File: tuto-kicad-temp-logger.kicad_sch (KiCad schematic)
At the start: 0 parts

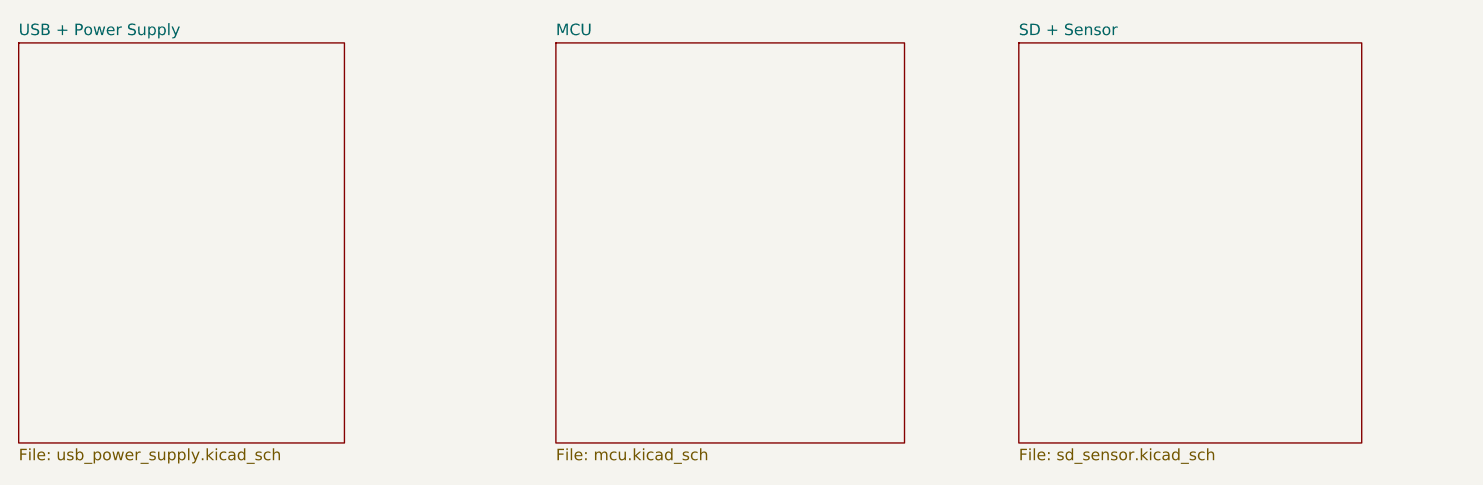
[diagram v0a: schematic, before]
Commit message: Connexion des pages du schéma
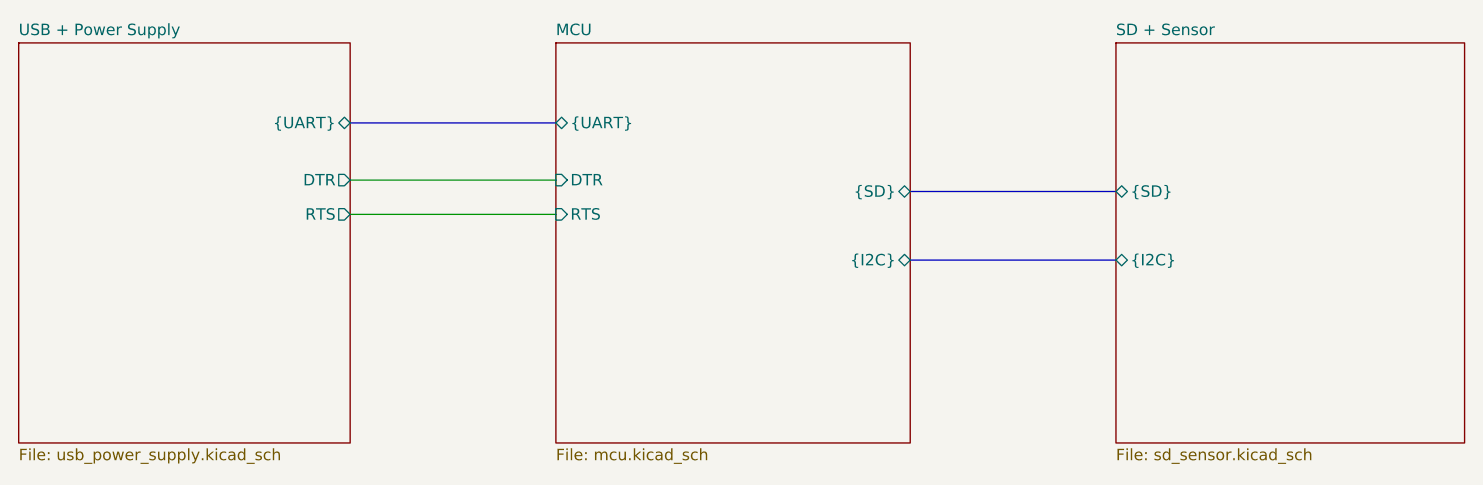
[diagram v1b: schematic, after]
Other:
- sheet MCU ports: added DTR, RTS, {I2C}, {SD}, {UART}; removed none
- sheet SD + Sensor ports: added {I2C}, {SD}; removed none
- sheet USB + Power Supply ports: added DTR, RTS, {UART}; removed none
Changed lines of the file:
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@@
 		(company "pull-up.dev")
+	)
+	(wire
+		(pts
+			(xy 85.09 87.63) (xy 107.95 87.63)
+		)
+		(stroke
+			(width 0)
+			(type default)
+		)
+	)
+	(bus
+		(pts
+			(xy 147.32 92.71) (xy 170.18 92.71)
+		)
+		(stroke
+			(width 0)
+			(type default)
+		)
+	)
+	(bus
+		(pts
+			(xy 147.32 85.09) (xy 170.18 85.09)
+		)
+		(stroke
+			(width 0)
+			(type default)
+		)
+	)
+	(bus
+		(pts
+			(xy 85.09 77.47) (xy 107.95 77.47)
+		)
+		(stroke
+			(width 0)
+			(type default)
+		)
+	)
+	(wire
+		(pts
+			(xy 85.09 83.82) (xy 107.95 83.82)
+		)
+		(stroke
+			(width 0)
+			(type default)
+		)
 	)
 	(sheet
 		(at 48.26 68.58)
-		(size 36.195 44.45)
+		(size 36.83 44.45)
 		(fields_autoplaced yes)
 		(stroke
@@
 				)
 				(justify left top)
+			)
+		)
+		(pin "{UART}" bidirectional
+			(at 85.09 77.47 0)
+			(effects
+				(font
+					(size 1.27 1.27)
+				)
+				(justify right)
+			)
+		)
+		(pin "DTR" output
+			(at 85.09 83.82 0)
+			(effects
+				(font
+					(size 1.27 1.27)
+				)
+				(justify right)
+			)
+		)
+		(pin "RTS" output
+			(at 85.09 87.63 0)
+			(effects
+				(font
+					(size 1.27 1.27)
+				)
+				(justify right)
 			)
 		)
@@
 	(sheet
 		(at 107.95 68.58)
-		(size 38.735 44.45)
+		(size 39.37 44.45)
 		(fields_autoplaced yes)
 		(stroke
@@
 				)
 				(justify left top)
+			)
+		)
+		(pin "RTS" input
+			(at 107.95 87.63 180)
+			(effects
+				(font
+					(size 1.27 1.27)
+				)
+				(justify left)
+			)
+		)
+		(pin "DTR" input
+			(at 107.95 83.82 180)
+			(effects
+				(font
+					(size 1.27 1.27)
+				)
+				(justify left)
+			)
+		)
+		(pin "{SD}" bidirectional
+			(at 147.32 85.09 0)
+			(effects
+				(font
+					(size 1.27 1.27)
+				)
+				(justify right)
+			)
+		)
+		(pin "{UART}" bidirectional
+			(at 107.95 77.47 180)
+			(effects
+				(font
+					(size 1.27 1.27)
+				)
+				(justify left)
+			)
+		)
+		(pin "{I2C}" bidirectional
+			(at 147.32 92.71 0)
+			(effects
+				(font
+					(size 1.27 1.27)
+				)
+				(justify right)
 			)
 		)
@@
 	)
 	(sheet
-		(at 159.385 68.58)
-		(size 38.1 44.45)
+		(at 170.18 68.58)
+		(size 38.735 44.45)
 		(fields_autoplaced yes)
 		(stroke
@@
 		)
 		(property "Sheetname" "SD + Sensor"
-			(at 159.385 67.8684 0)
+			(at 170.18 67.8684 0)
 			(effects
 				(font
@@
 		)
 		(property "Sheetfile" "sd_sensor.kicad_sch"
-			(at 159.385 113.6146 0)
+			(at 170.18 113.6146 0)
 			(effects
 				(font
@@
 			)
 		)
+		(pin "{SD}" bidirectional
+			(at 170.18 85.09 180)
+			(effects
+				(font
+					(size 1.27 1.27)
+				)
+				(justify left)
+			)
+		)
+		(pin "{I2C}" bidirectional
+			(at 170.18 92.71 180)
+			(effects
+				(font
+					(size 1.27 1.27)
+				)
+				(justify left)
+			)
+		)

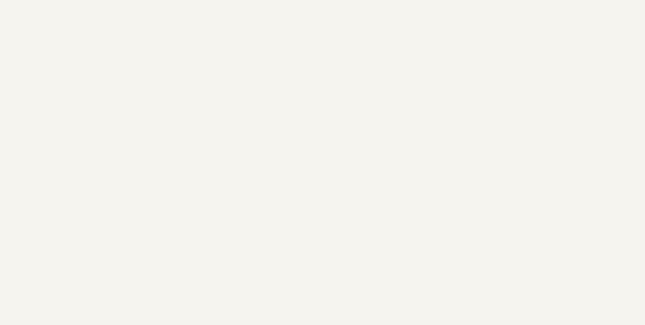
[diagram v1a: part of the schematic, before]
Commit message: Placement des composants
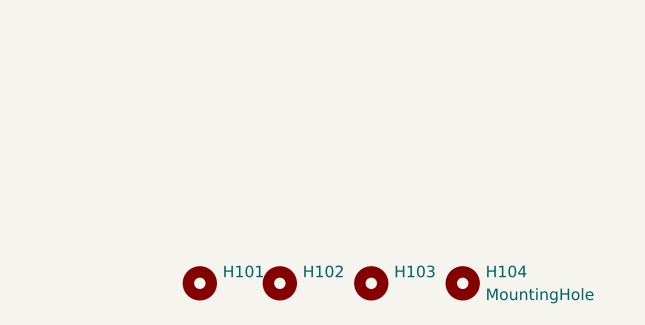
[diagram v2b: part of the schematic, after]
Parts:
- added H101, H102, H103, H104: MountingHole, MountingHole:MountingHole_4.3mm_M4, symbol Mechanical:MountingHole
